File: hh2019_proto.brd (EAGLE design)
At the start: 263.1 x 150 mm, 145 parts, among them IC1 CP210X_USB_UART, IC2 AP2114H, IC4 TP4056, J1 PJ-313D, Q1 MMBT2222A, Q3 MMBT2222A, Q4 MMBT2222A, Q5 SI1304 BDL, U1 MPR121QR2, U2 ESP32-WROVER-I, U3 PCM5102A, X4 JST-PH3

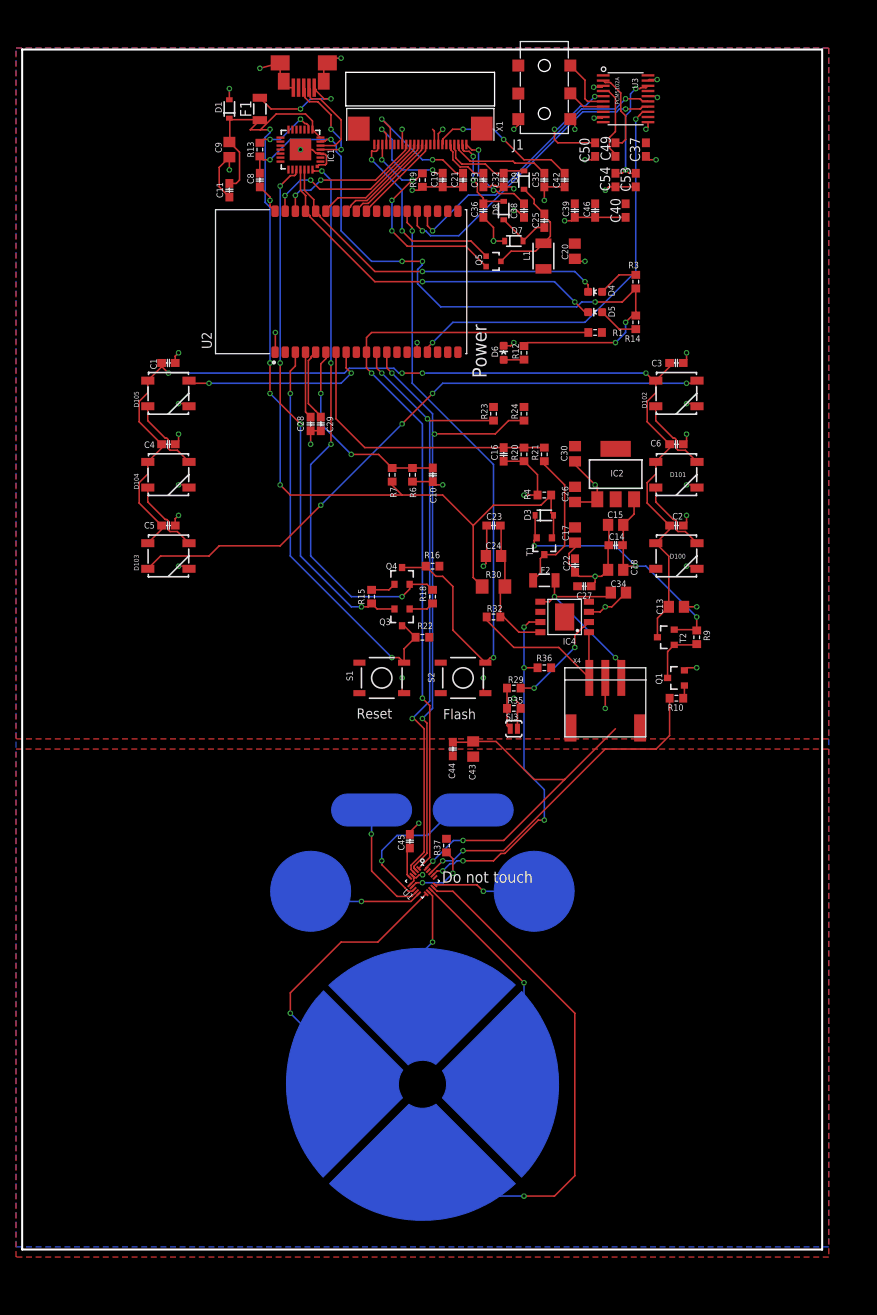
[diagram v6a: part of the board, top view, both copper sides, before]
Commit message: Shrunk PCB dimensions, added version and credits
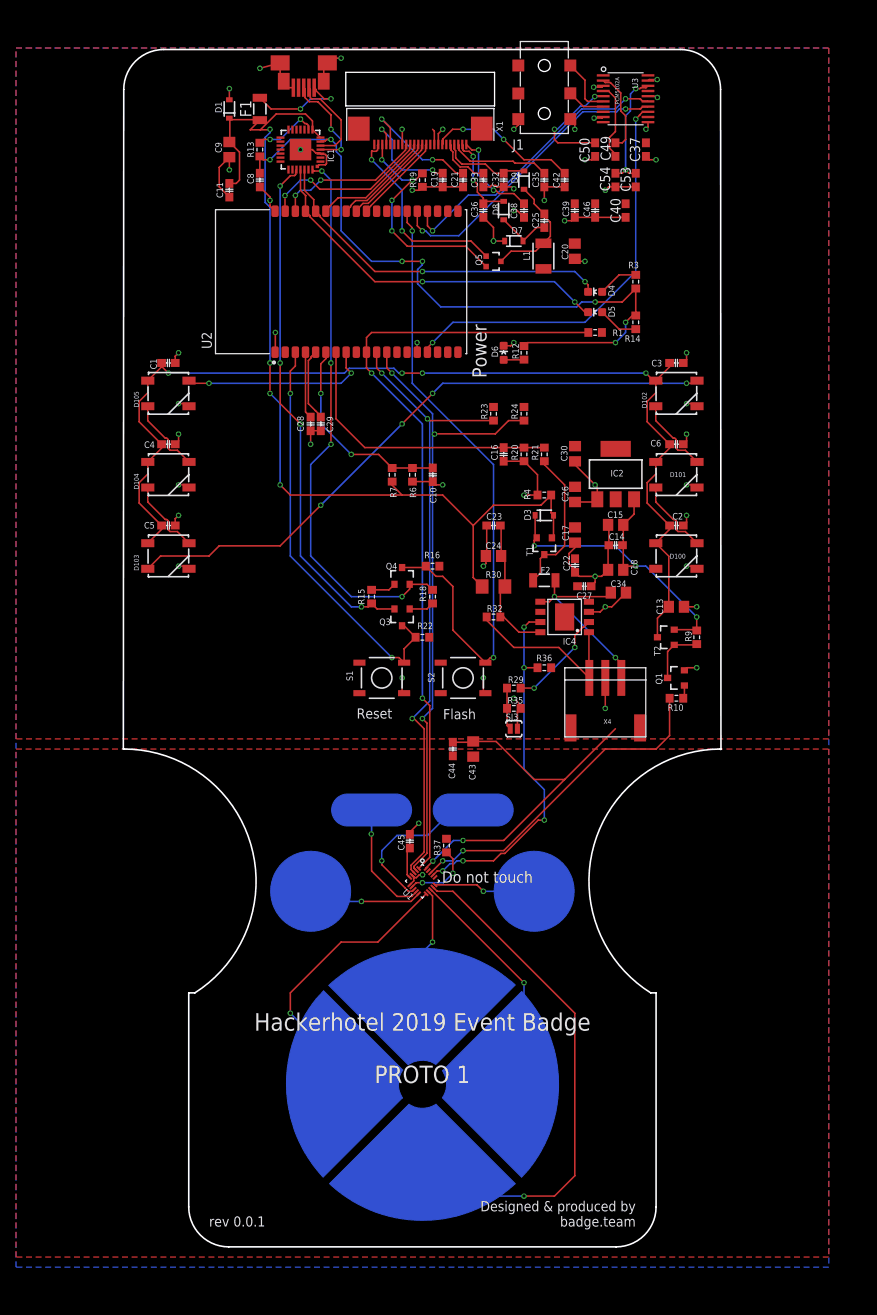
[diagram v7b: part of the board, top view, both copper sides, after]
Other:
- board size 263.1 x 150 mm -> 250.5 x 149.7 mm
- board text added: "Designed & produced by badge.team"
- board text added: "Hackerhotel 2019 Event Badge PROTO 1"
- board text added: "rev 0.0.1"
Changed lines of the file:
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@@
 <dimension x1="10" y1="-1" x2="85" y2="-1" x3="47.5" y3="-11.2972" textsize="2.54" layer="48" visible="yes"/>
 <dimension x1="10" y1="-1" x2="47.5068" y2="-1.0004" x3="28.754553125" y3="107.23805625" textsize="2.54" layer="48" visible="yes"/>
-<text x="14.86" y="15.4456" size="2.54" layer="26" font="vector" ratio="15" rot="MR45" align="top-center">B</text>
-<text x="4.6364" y="24.7664" size="2.54" layer="26" font="vector" ratio="15" rot="MR45" align="top-center">A</text>
+<text x="-28.32" y="53.5456" size="2.54" layer="26" font="vector" ratio="15" rot="MR45" align="top-center">B</text>
+<text x="-33.4636" y="53.9764" size="2.54" layer="26" font="vector" ratio="15" rot="MR45" align="top-center">A</text>
 <polygon width="0.4064" layer="26">
 <vertex x="-121.8" y="19.4" curve="90"/>
@@
 <vertex x="-118.9" y="19.4"/>
 </polygon>
-<circle x="20" y="20" radius="5.3851625" width="0" layer="26"/>
-<circle x="10" y="29" radius="5.09901875" width="0" layer="22"/>
-<text x="30.86" y="7.4456" size="2.54" layer="26" font="vector" ratio="15" rot="MR45" align="top-center">Start</text>
-<text x="44.86" y="7.4456" size="2.54" layer="26" font="vector" ratio="15" rot="MR45" align="top-center">Select</text>
-<wire x1="31" y1="11" x2="35" y2="7" width="4.5" layer="26"/>
+<circle x="-107.9" y="40.7" radius="5.3851625" width="0" layer="26"/>
+<circle x="-135.95" y="40.63" radius="5.09901875" width="0" layer="22"/>
+<text x="68.96" y="3.6356" size="2.54" layer="26" font="vector" ratio="15" rot="MR45" align="top-center">Start</text>
+<text x="71.53" y="11.2556" size="2.54" layer="26" font="vector" ratio="15" rot="MR45" align="top-center">Select</text>
+<wire x1="28.46" y1="8.46" x2="32.46" y2="4.46" width="4.5" layer="26"/>
 <wire x1="45.565" y1="11.355" x2="49.565" y2="7.355" width="4.5" layer="26"/>
 <text x="-119.48" y="41.71" size="1.4224" layer="25" font="vector" ratio="15">Do not touch</text>
-<wire x1="-171.95" y1="-4.14" x2="-71.95" y2="-4.14" width="0.254" layer="20"/>
-<wire x1="-71.95" y1="-4.14" x2="-71.95" y2="145.86" width="0.254" layer="20"/>
-<wire x1="-171.95" y1="-4.14" x2="-171.95" y2="145.86" width="0.254" layer="20"/>
-<wire x1="-171.95" y1="145.86" x2="-71.95" y2="145.86" width="0.254" layer="20"/>
+<wire x1="-159.3" y1="58.4" x2="-159.25285625" y2="140.863846875" width="0.2" layer="20"/>
+<wire x1="-159.25285625" y1="140.863846875" x2="-154.25285625" y2="145.86" width="0.2" layer="20" curve="-89.967234"/>
+<wire x1="-154.25285625" y1="145.86" x2="-89.647146875" y2="145.86" width="0.2" layer="20"/>
+<wire x1="-89.647146875" y1="145.86" x2="-84.647146875" y2="140.86360625" width="0.2" layer="20" curve="-89.958675"/>
+<wire x1="-84.647146875" y1="140.86360625" x2="-84.6" y2="58.4" width="0.2" layer="20"/>
 <polygon width="0.2" layer="42">
 <vertex x="-147.82" y="125.83"/>
@@
 <text x="-113.9" y="104.8" size="1.778" layer="25" rot="R90">Power</text>
 <text x="-143.3" y="137.4" size="1.4224" layer="25" rot="R90">F1</text>
+<wire x1="-159.25" y1="58.42" x2="-150.36" y2="27.94" width="0.2" layer="20" curve="-147.528808"/>
+<wire x1="-84.69" y1="58.42" x2="-93.38" y2="27.94" width="0.2" layer="20" curve="147.528808"/>
+<wire x1="-151.13" y1="27.94" x2="-151.13" y2="1.19" width="0.2" layer="20"/>
+<wire x1="-151.13" y1="1.19" x2="-146.13" y2="-3.81" width="0.2" layer="20" curve="90"/>
+<wire x1="-146.13" y1="-3.81" x2="-97.71" y2="-3.81" width="0.2" layer="20"/>
+<wire x1="-97.71" y1="-3.81" x2="-92.71" y2="1.19" width="0.2" layer="20" curve="90"/>
+<wire x1="-92.71" y1="1.19" x2="-92.71" y2="27.94" width="0.2" layer="20"/>
+<wire x1="-151.13" y1="27.94" x2="-150.36" y2="27.94" width="0.2" layer="20"/>
+<wire x1="-92.71" y1="27.94" x2="-93.38" y2="27.94" width="0.2" layer="20"/>
+<rectangle x1="-132.08" y1="49.53" x2="-124.46" y2="52.07" layer="26"/>
+<rectangle x1="-119.38" y1="49.53" x2="-111.76" y2="52.07" layer="26"/>
+<text x="-121.92" y="25.4" size="2.1844" layer="25" font="vector" align="top-center">Hackerhotel 2019 Event Badge
+PROTO 1</text>
+<text x="-148.59" y="-1.27" size="1.27" layer="25">rev 0.0.1</text>
+<text x="-95.25" y="-1.27" size="1.27" layer="25" align="bottom-right">Designed &amp; produced by
+badge.team</text>
+<wire x1="-84.6" y1="58.4" x2="-84.69" y2="58.42" width="0.2" layer="20" curve="-180"/>
+<wire x1="-159.3" y1="58.4" x2="-159.25" y2="58.42" width="0.2" layer="20" curve="-180"/>
 </plain>
 <attributes>
@@
 </element>
 <element name="R9" library="00ralf" package="R0603-DASHES" value="10k" x="-87.63" y="72.39" smashed="yes" rot="R90">
-<attribute name="NAME" x="-86.781" y="73.279" size="0.8128" layer="25" font="vector" ratio="16" rot="R270"/>
+<attribute name="NAME" x="-89.081" y="73.179" size="0.8128" layer="25" font="vector" ratio="16" rot="R270"/>
 <attribute name="PARTNO" value="ERJ-3GEYJ103V" x="-87.63" y="72.39" size="1.778" layer="27" rot="R90" display="off"/>
 <attribute name="VALUE" x="-85.598" y="71.501" size="1.27" layer="27" rot="R90"/>
@@
 </element>
 <element name="X4" library="badge" package="JST-PH3" value="JST-PH3" x="-99.06" y="67.31" smashed="yes" rot="R180">
-<attribute name="NAME" x="-102.104" y="69.774" size="0.6096" layer="21" font="vector" ratio="16" rot="R180"/>
+<attribute name="NAME" x="-98.294" y="62.154" size="0.6096" layer="21" font="vector" ratio="16" rot="R180"/>
 </element>
 <element name="C23" library="hh2019_proto" package="C0603-DASHES" value="100n" x="-113.03" y="86.36" smashed="yes">
@@
 </element>
 <element name="T2" library="SparkFun-DiscreteSemi" package="SOT23-3" value="" x="-91.44" y="72.39" smashed="yes" rot="R90">
-<attribute name="NAME" x="-89.762" y="72.9155" size="0.8128" layer="25" font="vector" ratio="16" rot="R270"/>
+<attribute name="NAME" x="-92.962" y="71.3155" size="0.8128" layer="25" font="vector" ratio="16" rot="R270"/>
 <attribute name="PARTNO" value="" x="-91.44" y="72.39" size="1.778" layer="27" rot="R90" display="off"/>
 <attribute name="PROD_ID" value="TRANS-08285" x="-91.44" y="72.39" size="1.778" layer="27" rot="R90" display="off"/>
@@
 <vertex x="-172.72" y="146.05"/>
 <vertex x="-71.12" y="146.05"/>
-<vertex x="-71.12" y="-3.81"/>
-<vertex x="-172.72" y="-3.81"/>
+<vertex x="-71.12" y="-6.35"/>
+<vertex x="-172.72" y="-6.35"/>
 </polygon>
 <wire x1="-138.05" y1="141.09" x2="-139.25" y2="141.09" width="0.2" layer="1"/>
@@
 </drawing>
 <compatibility>
+<note version="6.3" minversion="6.2.2" severity="warning">
+Since Version 6.2.2 text objects can contain more than one line,
+which will not be processed correctly with this version.
+</note>
 <note version="8.2" severity="warning">
 Since Version 8.2, EAGLE supports online libraries. The ids

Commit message: Added missing DAC connections. Fixes #1
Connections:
- new net +3V3: U3.P$17
- net GND: now also U3.P$12
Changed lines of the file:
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@@
 <wire x1="-109.93" y1="136.45" x2="-110.49" y2="135.89" width="0.2" layer="1"/>
 <via x="-110.49" y="135.89" extent="1-16" drill="0.4"/>
+<contactref element="U3" pad="P$12"/>
 <wire x1="123.19" y1="72.39" x2="133.35" y2="72.39" width="0" layer="19" extent="1-1"/>
 <wire x1="114.3" y1="72.39" x2="123.19" y2="72.39" width="0" layer="19" extent="1-1"/>
@@
 <wire x1="104.14" y1="20.32" x2="114.3" y2="20.32" width="0" layer="19" extent="1-1"/>
 <wire x1="95.25" y1="20.32" x2="104.14" y2="20.32" width="0" layer="19" extent="1-1"/>
-<wire x1="-87.63" y1="76.2" x2="95.25" y2="72.39" width="0" layer="19" extent="1-1"/>
+<wire x1="-87.63" y1="68.58" x2="95.25" y2="72.39" width="0" layer="19" extent="1-1"/>
+<wire x1="-87.63" y1="76.2" x2="-87.63" y2="68.58" width="0" layer="19" extent="1-1"/>
+<wire x1="-87.593" y1="80.95" x2="-87.63" y2="76.2" width="0" layer="19" extent="1-1"/>
+<wire x1="-89.32" y1="86.36" x2="-88.9" y2="81.28" width="0" layer="19" extent="1-1"/>
+<wire x1="-87.593" y1="91.11" x2="-88.9" y2="87.63" width="0" layer="19" extent="1-1"/>
+<wire x1="-89.32" y1="96.52" x2="-88.9" y2="91.44" width="0" layer="19" extent="1-1"/>
+<wire x1="-87.593" y1="101.27" x2="-88.9" y2="97.79" width="0" layer="19" extent="1-1"/>
+<wire x1="-89.32" y1="106.68" x2="-88.9" y2="101.6" width="0" layer="19" extent="1-1"/>
+<wire x1="-96.47" y1="77.97" x2="-89.22" y2="76.2" width="0" layer="19" extent="1-1"/>
+<wire x1="-100.83" y1="78.77" x2="-99.06" y2="76.2" width="0" layer="19" extent="1-1"/>
+<wire x1="-100.4" y1="89.3" x2="-98.71" y2="86.44" width="0" layer="19" extent="1-1"/>
+<wire x1="-107.53" y1="90.17" x2="-102.84" y2="89.3" width="0" layer="19" extent="1-1"/>
+<wire x1="-113.88" y1="86.36" x2="-109.22" y2="90.17" width="0" layer="19" extent="1-1"/>
+<wire x1="-119.38" y1="91.44" x2="-113.88" y2="86.36" width="0" layer="19" extent="1-1"/>
+<wire x1="-99.06" y1="67.31" x2="-99.695" y2="75.565" width="0" layer="19" extent="1-1"/>
+<wire x1="-109.64" y1="63.5" x2="-99.06" y2="63.5" width="0" layer="19" extent="1-1"/>
+<wire x1="-114.046" y1="65.405" x2="-110.49" y2="64.77" width="0" layer="19" extent="1-1"/>
+<wire x1="-115.57" y1="57.47" x2="-110.04" y2="60.96" width="0" layer="19" extent="1-1"/>
+<wire x1="-118.11" y1="57.57" x2="-115.57" y2="57.47" width="0" layer="19" extent="1-1"/>
+<wire x1="-122.368240625" y1="49.15075625" x2="-118.11" y2="57.57" width="0" layer="19" extent="1-1"/>
+<wire x1="-118.91" y1="47.2" x2="-122.368240625" y2="49.15075625" width="0" layer="19" extent="1-1"/>
+<wire x1="-123.231115625" y1="42.646378125" x2="-123.49" y2="47.75" width="0" layer="19" extent="1-1"/>
+<wire x1="-124.206" y1="65.405" x2="-114.3" y2="65.659" width="0" layer="19" extent="1-1"/>
+<wire x1="-134.62" y1="98.21" x2="-123.16" y2="91.85" width="0" layer="19" extent="1-1"/>
+<wire x1="-140.34" y1="108.03" x2="-135.89" y2="98.21" width="0" layer="19" extent="1-1"/>
+<wire x1="-152.4" y1="107.95" x2="-140.34" y2="108.03" width="0" layer="19" extent="1-1"/>
+<wire x1="-152.4" y1="101.6" x2="-152.82" y2="106.68" width="0" layer="19" extent="1-1"/>
+<wire x1="-152.4" y1="97.79" x2="-151.093" y2="101.27" width="0" layer="19" extent="1-1"/>
+<wire x1="-152.4" y1="91.44" x2="-152.82" y2="96.52" width="0" layer="19" extent="1-1"/>
+<wire x1="-152.4" y1="87.63" x2="-151.093" y2="91.11" width="0" layer="19" extent="1-1"/>
+<wire x1="-152.4" y1="81.28" x2="-152.82" y2="86.36" width="0" layer="19" extent="1-1"/>
+<wire x1="-111.76" y1="108.827" x2="-111.76" y2="94.4" width="0" layer="19" extent="1-1"/>
+<wire x1="-122.56" y1="108.03" x2="-111.76" y2="108.827" width="0" layer="19" extent="1-1"/>
+<wire x1="-111.64" y1="121.92" x2="-110.49" y2="109.22" width="0" layer="19" extent="1-1"/>
+<wire x1="-110.49" y1="125.73" x2="-113.03" y2="123.61" width="0" layer="19" extent="1-1"/>
+<wire x1="-110.49" y1="128.4548" x2="-110.49" y2="125.73" width="0" layer="19" extent="1-1"/>
+<wire x1="-116.84" y1="128.69" x2="-114.3" y2="128.69" width="0" layer="19" extent="1-1"/>
+<wire x1="-106.68" y1="127" x2="-109.22" y2="124.88" width="0" layer="19" extent="1-1"/>
+<wire x1="-104.14" y1="124.46" x2="-106.68" y2="127" width="0" layer="19" extent="1-1"/>
+<wire x1="-99.06" y1="128.27" x2="-100.33" y2="124.88" width="0" layer="19" extent="1-1"/>
+<wire x1="-93.56" y1="132.08" x2="-95.25" y2="128.69" width="0" layer="19" extent="1-1"/>
+<wire x1="-93.98" y1="135.89" x2="-93.98" y2="132.5" width="0" layer="19" extent="1-1"/>
+<wire x1="-93.72" y1="137.425" x2="-93.72" y2="136.775" width="0" layer="19" extent="1-1"/>
+<wire x1="-93.72" y1="140.025" x2="-93.72" y2="137.425" width="0" layer="19" extent="1-1"/>
+<wire x1="-93.72" y1="141.975" x2="-93.72" y2="140.025" width="0" layer="19" extent="1-1"/>
+<wire x1="-100.75" y1="132.08" x2="-98.64" y2="128.69" width="0" layer="19" extent="1-1"/>
+<wire x1="-102.87" y1="135.89" x2="-101.6" y2="132.08" width="0" layer="19" extent="1-1"/>
+<wire x1="-100.464446875" y1="137.294446875" x2="-102.87" y2="136.6" width="0" layer="19" extent="1-1"/>
+<wire x1="-99.495553125" y1="141.149446875" x2="-99.32" y2="137.425" width="0" layer="19" extent="1-1"/>
+<wire x1="-102.87" y1="119.7" x2="-103.29" y2="124.46" width="0" layer="19" extent="1-1"/>
+<wire x1="-119.93" y1="133.99" x2="-119.38" y2="128.69" width="0" layer="19" extent="1-1"/>
+<wire x1="-124.43" y1="133.99" x2="-119.93" y2="133.99" width="0" layer="19" extent="1-1"/>
+<wire x1="-109.93" y1="137.16" x2="-103.43" y2="137.16" width="0" layer="19" extent="1-1"/>
+<wire x1="-133.9076" y1="132.60455" x2="-124.43" y2="133.99" width="0" layer="19" extent="1-1"/>
+<wire x1="-142.24" y1="128.69" x2="-137.16" y2="133.35" width="0" layer="19" extent="1-1"/>
+<wire x1="-146.05" y1="127.42" x2="-142.24" y2="128.69" width="0" layer="19" extent="1-1"/>
+<wire x1="-146.05" y1="139.58" x2="-146.05" y2="132.4" width="0" layer="19" extent="1-1"/>
+<wire x1="-142.24" y1="143.51" x2="-146.05" y2="140.97" width="0" layer="19" extent="1-1"/>
+<wire x1="-134.25" y1="141.89" x2="-138.05" y2="141.09" width="0" layer="19" extent="1-1"/>
 </signal>
 <signal name="USB_DN_CON">
@@
 <wire x1="-106.045" y1="76.835" x2="-107.175" y2="76.835" width="0.2" layer="1"/>
 </signal>
+<signal name="+3V3">
+<contactref element="U3" pad="P$17"/>
+</signal>
 </signals>
